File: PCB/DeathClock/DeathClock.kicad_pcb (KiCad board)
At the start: 2 copper layers, 37.2 x 31.2 mm, 27 parts, among them J1 Conn_01x05_Female, J2 EDP_24pin_conn FFC2B35-24-T, Q1 MCH3478, U1 STM32L010F4P6, Y1 Crystal

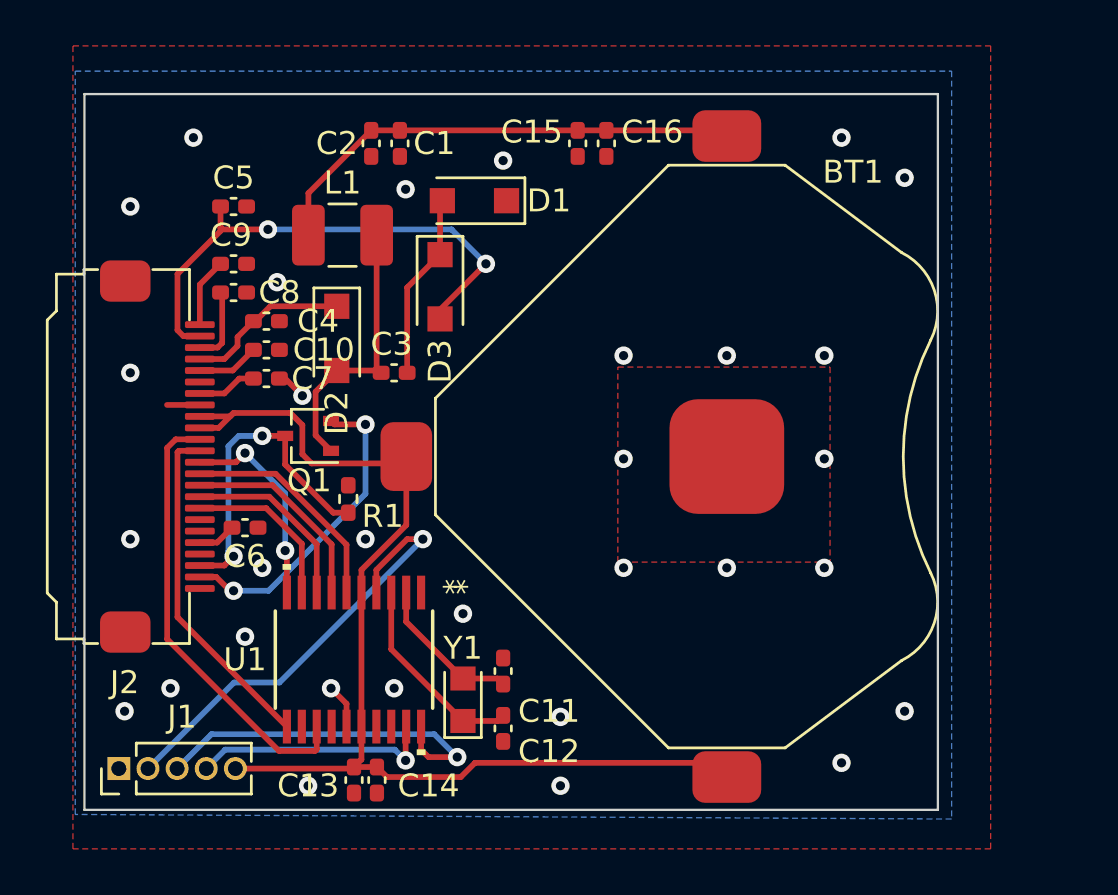
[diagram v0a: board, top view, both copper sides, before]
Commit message: added second mosfet to toggle epd power
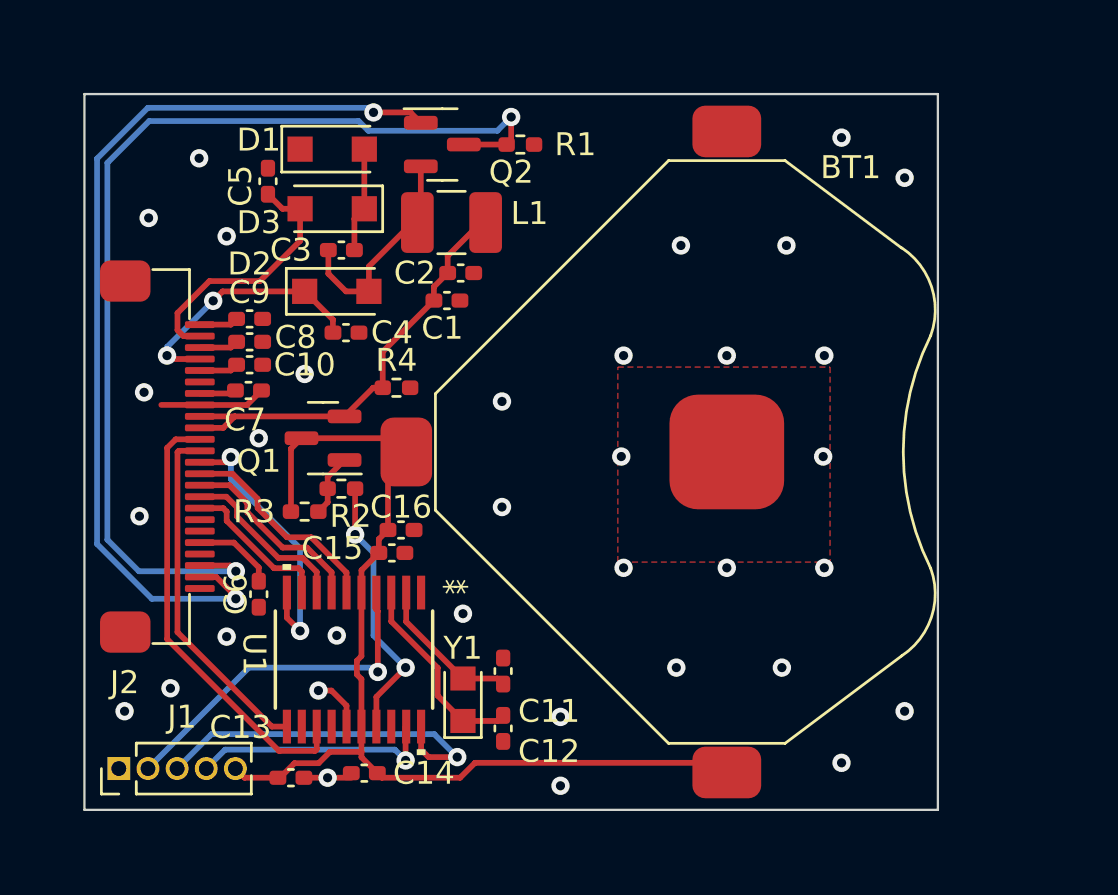
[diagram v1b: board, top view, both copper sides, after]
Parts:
- added Q2: PJA3430_R1_00001, Package_TO_SOT_SMD:SOT-23, F.Cu at (133.6, 71.8)
- added R2: 1, Resistor_SMD:R_0402_1005Metric_Pad0.72x0.64mm_HandSolder, F.Cu at (129.2, 86.8)
- added R3: 10k, Resistor_SMD:R_0402_1005Metric_Pad0.72x0.64mm_HandSolder, F.Cu at (127.6, 87.8)
- added R4: 100k, Resistor_SMD:R_0402_1005Metric_Pad0.72x0.64mm_HandSolder, F.Cu at (131.6, 82.4)
- L1: value ATNR4010100MT -> 10uH ±20% 0.8A 1276AS-H-100M=P2
- Q1: value MCH3478 -> PJA3431_R1_00001; footprint Package_TO_SOT_SMD:SOT-323_SC-70 -> Package_TO_SOT_SMD:SOT-23
- moved C15 19.6 mm to (131.4, 89.6), turned to 180 degrees
- moved C16 19.1 mm to (131.8, 88.6), turned to 180 degrees
- moved R1 17.2 mm to (137.0, 71.8), turned to 180 degrees
- moved C1 7.15 mm to (133.8, 78.6), turned to 0 degrees
- moved C2 6.87 mm to (134.4, 77.4), turned to 0 degrees
- moved D1 6.60 mm to (128.8, 72.0), turned to 0 degrees
- moved C3 5.82 mm to (129.2, 76.4)
- moved D3 5.80 mm to (128.8, 74.6), turned to 180 degrees
- moved L1 4.78 mm to (134.0, 75.2), turned to 180 degrees
- moved C4 3.50 mm to (129.4, 80.0)
- moved C6 2.96 mm to (125.6, 91.4), turned to 90 degrees
- moved C13 2.75 mm to (127.0, 99.4), turned to 180 degrees
- moved C9 2.50 mm to (125.2, 79.4)
- moved C8 2.26 mm to (125.2, 80.4)
- moved D2 2.05 mm to (129.0, 78.2), turned to 0 degrees
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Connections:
- C1 pad 1: VCC -> edpVCC
- C2 pad 1: VCC -> edpVCC
- J2 pad 15: VCC -> edpVCC
- J2 pad 16: VCC -> edpVCC
- J2 pad 2: Net-(Q1-Pad2) -> Net-(J2-Pad2)
- J2 pad 3: Net-(Q1-Pad3) -> Net-(J2-Pad3)
- L1 pad 1: VCC -> edpVCC
- Q1 pad 1: Net-(C3-Pad2) -> Net-(Q1-Pad1)
- Q1 pad 2: Net-(Q1-Pad2) -> edpVCC
- Q1 pad 3: Net-(Q1-Pad3) -> VCC
- R1 pad 2: Net-(Q1-Pad3) -> Net-(J2-Pad3)
- U1 pad 17: unconnected-(U1-Pad17) -> /edp/VCC_Enable
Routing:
- net Net-(J2-Pad3): track 0.00 -> 46.2 mm, vias 0 -> 2
- net Net-(J2-Pad2): track 0.00 -> 41.2 mm, vias 0 -> 2
- net VCC: track 70.5 -> 45.4 mm
- net edpVCC: track 0.00 -> 19.5 mm
- net Net-(Q1-Pad3): track 14.1 -> 0.00 mm, vias 2 -> 0
- net Net-(Q1-Pad2): track 13.8 -> 0.00 mm, vias 2 -> 0
- net /edp/VCC_Enable: track 0.00 -> 11.8 mm, vias 0 -> 2
- net Net-(C5-Pad2): track 22.7 -> 11.5 mm, vias 2 -> 0
- net MCU_RESET: track 19.7 -> 15.4 mm
- net Net-(C4-Pad2): track 7.15 -> 11.2 mm, vias 0 -> 2
- net Net-(C3-Pad1): track 8.13 -> 4.58 mm
- net /edp/edp_spi_cs: track 8.97 -> 12.2 mm
- net Net-(Q1-Pad1): track 0.00 -> 2.72 mm
- net Net-(C3-Pad2): track 12.2 -> 9.51 mm
- net Net-(C6-Pad2): track 1.67 -> 3.62 mm
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
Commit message: made the coin cell symbol 4 pins to make drc happy
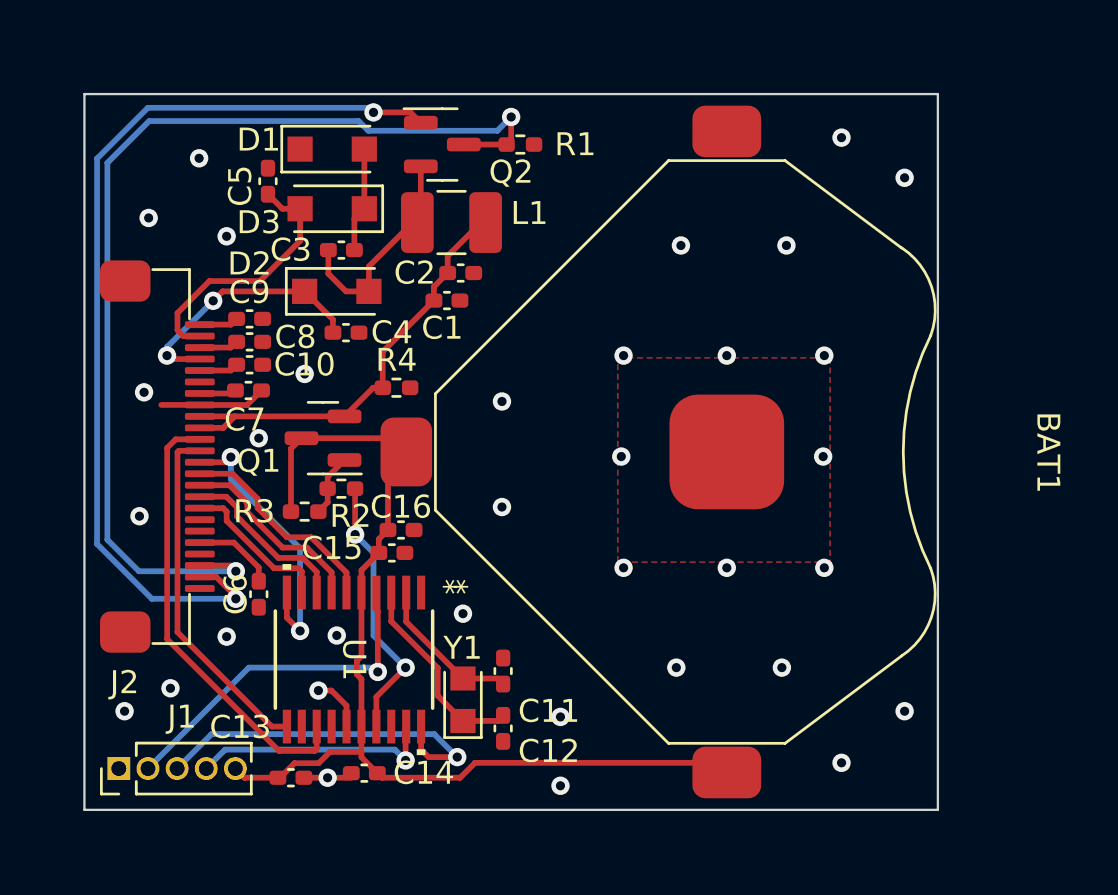
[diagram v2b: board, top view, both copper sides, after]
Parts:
- removed BT1: Battery_Cell, CoinCellHolder:AdamTech_CR2430_BH-109B-5
- added BAT1: AdamTech_CR2430_BH-109B-5, CoinCellHolder:AdamTech_CR2430_BH-109B-5_num_pads, F.Cu at (146.0, 85.2)
- C11, C12: value C -> 6pF
- C13, C15: value C -> 1uF
- C14, C16: value C -> 0.1uF

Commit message: moved some labels around and added SWD header pin names
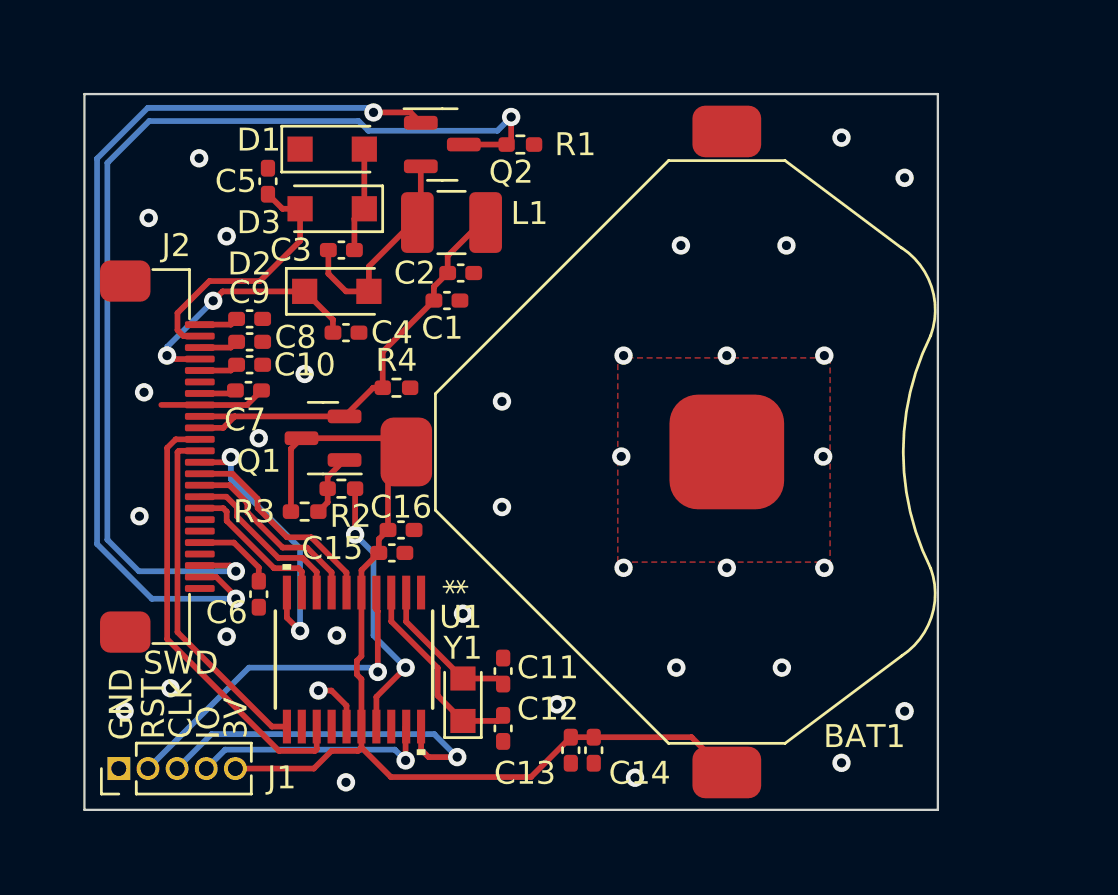
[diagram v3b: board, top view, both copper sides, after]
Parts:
- moved C13 12.3 mm to (139.2, 98.2), turned to 90 degrees
- moved C14 10.0 mm to (140.2, 98.2), turned to 90 degrees
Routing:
- net GND: track 9.11 -> 7.04 mm
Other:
- board text added: "3V"
- board text added: "CLK"
- board text added: "GND"
- board text added: "IO"
- board text added: "RST"
- board text added: "SWD"

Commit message: added silkscreen stuff for user-friendliness
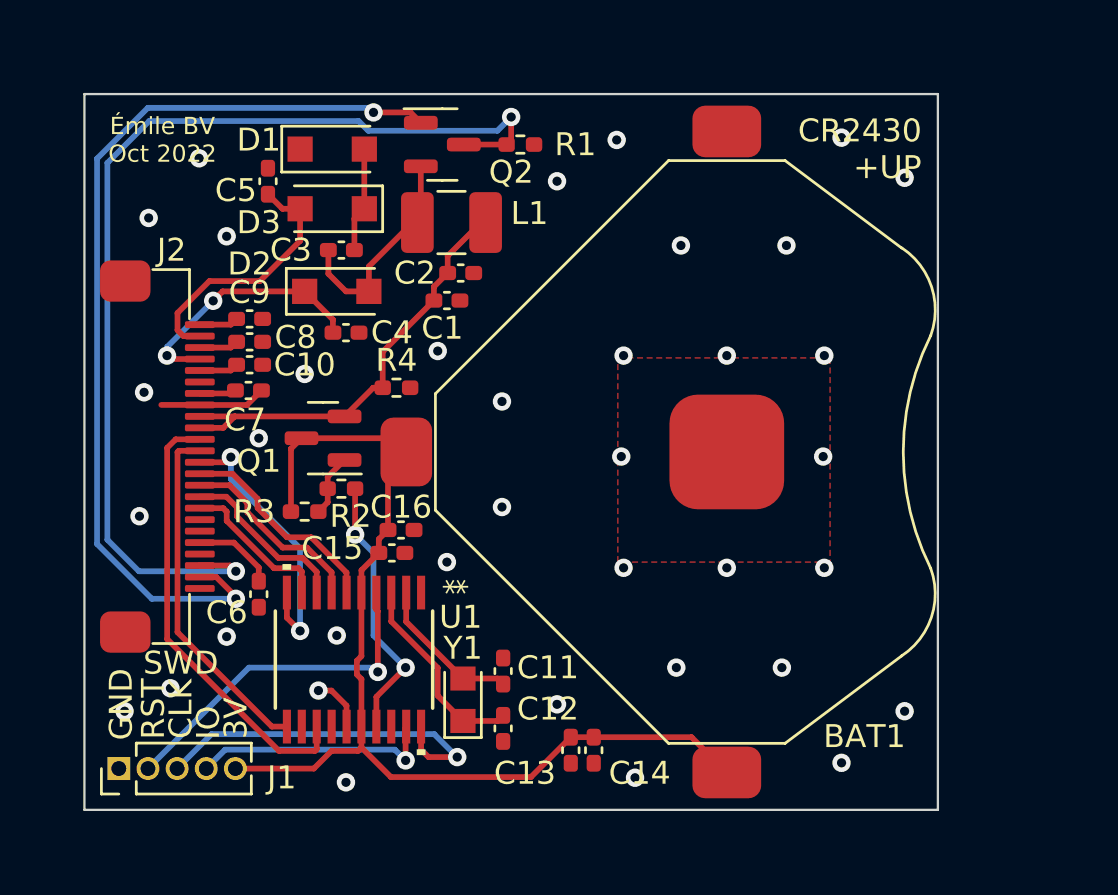
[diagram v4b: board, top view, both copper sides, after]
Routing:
- net GND: vias 34 -> 37
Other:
- board text added: "+UP"
- board text added: "CR2430"
- board text added: "Cable side"
- board text added: "Connect flat cable before putting double sided tape"
- board text added: "Kapton tape"
- board text added: "Émile BV Oct 2022"
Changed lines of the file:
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@@
 (kicad_pcb (version 20211014) (generator pcbnew)
   (general
-    (thickness 1.6)
+    (thickness 1)
   )
   (paper "A4")
@@
   )
   (setup
+    (stackup
+      (layer "F.SilkS" (type "Top Silk Screen") (color "White"))
+      (layer "F.Paste" (type "Top Solder Paste"))
+      (layer "F.Mask" (type "Top Solder Mask") (color "Black") (thickness 0.01))
+      (layer "F.Cu" (type "copper") (thickness 0.035))
+      (layer "dielectric 1" (type "core") (thickness 0.91) (material "FR4") (epsilon_r 4.5) (loss_tangent 0.02))
+      (layer "B.Cu" (type "copper") (thickness 0.035))
+      (layer "B.Mask" (type "Bottom Solder Mask") (color "Black") (thickness 0.01))
+      (layer "B.Paste" (type "Bottom Solder Paste"))
+      (layer "B.SilkS" (type "Bottom Silk Screen") (color "White"))
+      (copper_finish "None")
+      (dielectric_constraints no)
+    )
     (pad_to_mask_clearance 0)
     (pcbplotparams
@@
     (property "Sheetname" "edp")
     (attr smd)
-    (fp_text reference "J2" (at -9.2 0.38 unlocked) (layer "F.SilkS")
+    (fp_text reference "J2" (at -9 0.58 unlocked) (layer "F.SilkS")
       (effects (font (size 1 1) (thickness 0.15)))
     )
@@
     (property "Sheetname" "edp")
     (attr smd)
-    (fp_text reference "C5" (at 0 1.4 180) (layer "F.SilkS")
+    (fp_text reference "C5" (at 0.4 1.4 180) (layer "F.SilkS")
       (effects (font (size 1 1) (thickness 0.15)))
     )
@@
     )
   )
+  (gr_line (start 137.4 82) (end 138.8 79.2) (layer "B.SilkS") (width 0.15))
+  (gr_line (start 138.8 79.2) (end 140.2 82) (layer "B.SilkS") (width 0.15))
+  (gr_line (start 118.4 77.8) (end 119.4 77.8) (layer "B.SilkS") (width 0.15))
+  (gr_line (start 126 99.2) (end 126.4 98.8) (layer "B.SilkS") (width 0.15))
+  (gr_line (start 121.8 85.4) (end 120 85.4) (layer "B.SilkS") (width 0.15))
+  (gr_line (start 126 99.2) (end 126.4 99.6) (layer "B.SilkS") (width 0.15))
+  (gr_line (start 127.8 99.2) (end 126 99.2) (layer "B.SilkS") (width 0.15))
+  (gr_line (start 120 85.4) (end 120.4 85.8) (layer "B.SilkS") (width 0.15))
+  (gr_line (start 119.4 77.8) (end 119.4 93) (layer "B.SilkS") (width 0.15))
+  (gr_line (start 138.8 80.2) (end 138.8 81.2) (layer "B.SilkS") (width 0.15))
+  (gr_line (start 140.2 82) (end 137.4 82) (layer "B.SilkS") (width 0.15))
+  (gr_line (start 120 85.4) (end 120.4 85) (layer "B.SilkS") (width 0.15))
+  (gr_rect (start 144.4 82.4) (end 132.8 89.2) (layer "B.SilkS") (width 0.15) (fill none))
+  (gr_rect (start 118.6 100.2) (end 125.4 97.8) (layer "B.SilkS") (width 0.15) (fill none))
+  (gr_line (start 138.8 81.6) (end 138.8 81.6) (layer "B.SilkS") (width 0.15))
+  (gr_line (start 119.4 93) (end 118.4 93) (layer "B.SilkS") (width 0.15))
   (gr_rect (start 118 69.6) (end 155.2 100.8) (layer "Edge.Cuts") (width 0.1) (fill none))
+  (gr_text "Kapton tape\n" (at 132.6 99) (layer "B.SilkS")
+    (effects (font (size 1 1) (thickness 0.15)) (justify mirror))
+  )
+  (gr_text "Émile BV\nOct 2022" (at 149.6 73.2) (layer "B.SilkS")
+    (effects (font (size 1 1) (thickness 0.15)) (justify mirror))
+  )
+  (gr_text "Connect flat\ncable before\nputting double\nsided tape" (at 138.6 85.8) (layer "B.SilkS")
+    (effects (font (size 1 1) (thickness 0.15)) (justify mirror))
+  )
+  (gr_text "Cable side" (at 126 85.4) (layer "B.SilkS")
+    (effects (font (size 1 1) (thickness 0.15)) (justify mirror))
+  )
+  (gr_text "+UP" (at 153 72.8) (layer "F.SilkS")
+    (effects (font (size 1 1) (thickness 0.15)))
+  )
+  (gr_text "CR2430\n" (at 151.8 71.2) (layer "F.SilkS")
+    (effects (font (size 1 1) (thickness 0.15)))
+  )
   (gr_text "IO\n" (at 123.4 97 90) (layer "F.SilkS")
     (effects (font (size 1 1) (thickness 0.15)))
@@
   (gr_text "CLK\n" (at 122.2 96.4 90) (layer "F.SilkS")
     (effects (font (size 1 1) (thickness 0.15)))
+  )
+  (gr_text "Émile BV\nOct 2022" (at 121.4 71.6) (layer "F.SilkS")
+    (effects (font (size 0.75 0.75) (thickness 0.15)))
   )
   (segment (start 128.6325 77.4325) (end 128.6325 76.4) (width 0.25) (layer "F.Cu") (net 1))
@@
   (segment (start 128.2 95.6) (end 128.76742 95.6) (width 0.25) (layer "F.Cu") (net 4))
   (via (at 120.4 88) (size 0.8) (drill 0.4) (layers "F.Cu" "B.Cu") (free) (net 4))
-  (via (at 134.5 92.25) (size 0.8) (drill 0.4) (layers "F.Cu" "B.Cu") (net 4))
+  (via (at 133.8 90) (size 0.8) (drill 0.4) (layers "F.Cu" "B.Cu") (net 4))
   (via (at 138.6 96.2) (size 0.8) (drill 0.4) (layers "F.Cu" "B.Cu") (net 4))
+  (via (at 141.2 71.6) (size 0.8) (drill 0.4) (layers "F.Cu" "B.Cu") (net 4))
   (via (at 153.75 73.25) (size 0.8) (drill 0.4) (layers "F.Cu" "B.Cu") (net 4))
   (via (at 119.75 96.5) (size 0.8) (drill 0.4) (layers "F.Cu" "B.Cu") (net 4))
@@
   (via (at 151 98.75) (size 0.8) (drill 0.4) (layers "F.Cu" "B.Cu") (net 4))
   (via (at 144 76.2) (size 0.8) (drill 0.4) (layers "F.Cu" "B.Cu") (net 4))
+  (via (at 138.6 73.4) (size 0.8) (drill 0.4) (layers "F.Cu" "B.Cu") (net 4))
   (via (at 142 99.4) (size 0.8) (drill 0.4) (layers "F.Cu" "B.Cu") (net 4))
   (via (at 148.4 94.6) (size 0.8) (drill 0.4) (layers "F.Cu" "B.Cu") (net 4))
@@
   (via (at 136.2 87.6) (size 0.8) (drill 0.4) (layers "F.Cu" "B.Cu") (net 4))
   (via (at 123 72.4) (size 0.8) (drill 0.4) (layers "F.Cu" "B.Cu") (net 4))
+  (via (at 133.4 80.8) (size 0.8) (drill 0.4) (layers "F.Cu" "B.Cu") (net 4))
   (via (at 128.2 95.6) (size 0.8) (drill 0.4) (layers "F.Cu" "B.Cu") (net 4))
   (via (at 121.75 95.5) (size 0.8) (drill 0.4) (layers "F.Cu" "B.Cu") (net 4))
